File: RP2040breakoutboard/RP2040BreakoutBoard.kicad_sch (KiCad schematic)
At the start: 38 parts, among them J1 Conn_02x18_Odd_Even, J2 Conn_02x18_Odd_Even, J3 USB_C_Receptacle_USB2.0_14P, J4 Conn_01x02, U1 RP2040, U2 NCP1117-3.3_SOT223, U3 W25Q128JVS, X1 ABM8-272-T3

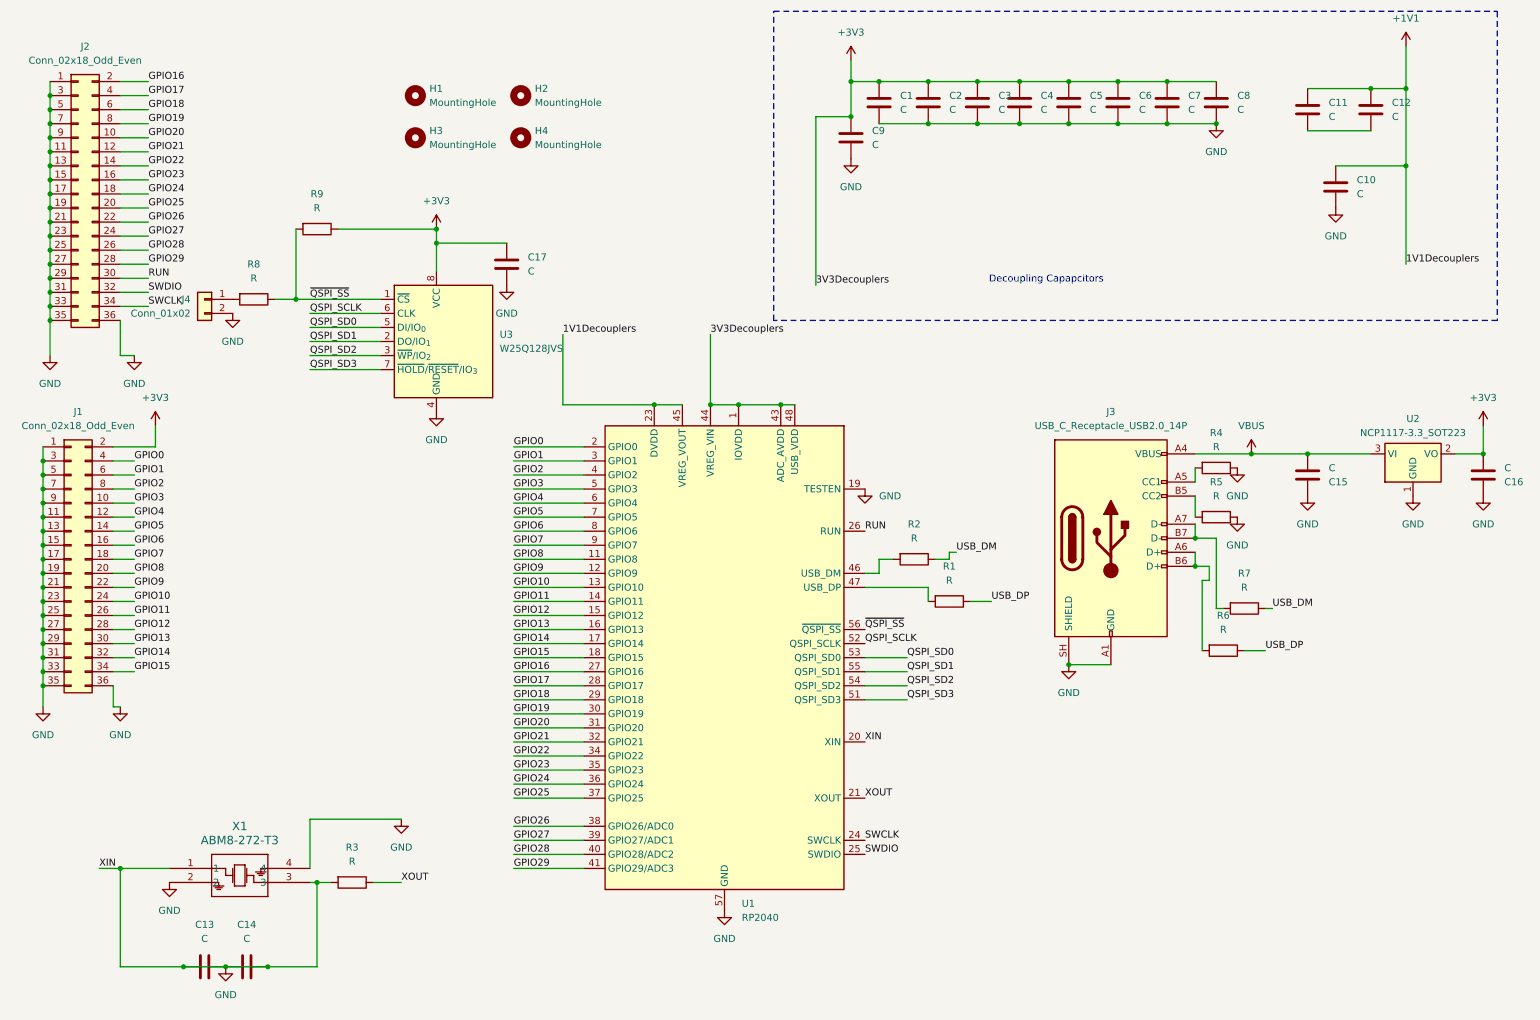
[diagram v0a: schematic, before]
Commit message: Tidied up schematic and assigned footprints
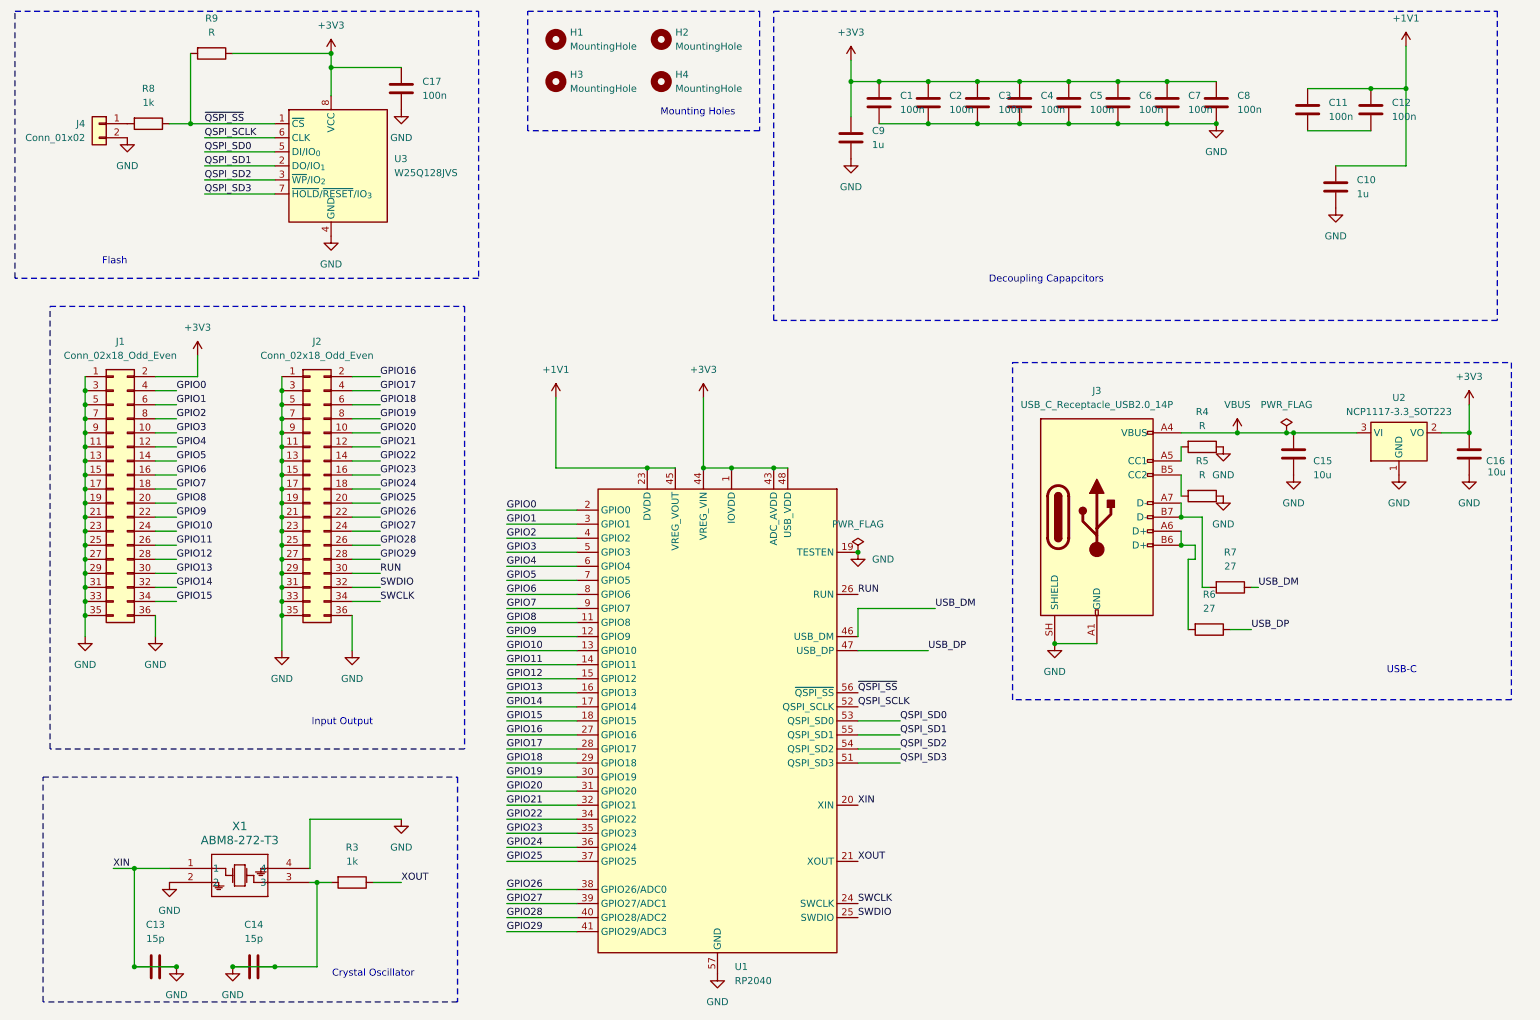
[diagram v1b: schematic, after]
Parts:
- removed R1, R2: R, symbol Device:R
- C1, C11, C12, C17, C2, C3, C4, C5, C6, C7, C8: value C -> 100n; footprint (none) -> Capacitor_SMD:C_0603_1608Metric
- C10, C9: value C -> 1u; footprint (none) -> Capacitor_SMD:C_0603_1608Metric
- C13, C14: value C -> 15p; footprint (none) -> Capacitor_SMD:C_0603_1608Metric
- C15, C16: value C -> 10u; footprint (none) -> Capacitor_SMD:C_0805_2012Metric
- H1, H2, H3, H4: footprint (none) -> MountingHole:MountingHole_3.2mm_M3
- J1, J2: footprint (none) -> Connector_PinHeader_2.54mm:PinHeader_2x18_P2.54mm_Vertical
- J3: footprint (none) -> Connector_USB:USB_C_Receptacle_GCT_USB4105-xx-A_16P_TopMnt_Horizontal
- J4: footprint (none) -> Connector_PinHeader_2.54mm:PinHeader_1x02_P2.54mm_Vertical
- R3, R8: value R -> 1k; footprint (none) -> Resistor_SMD:R_0603_1608Metric
- R4, R5, R9: footprint (none) -> Resistor_SMD:R_0603_1608Metric
- R6, R7: value R -> 27; footprint (none) -> Resistor_SMD:R_0603_1608Metric
- X1: footprint ABM8-272-T3_ABR -> Crystal:Crystal_SMD_3225-4Pin_3.2x2.5mm
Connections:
- net USB_DM: now also U1.46 (USB_DM)
- net USB_DP: now also U1.47 (USB_DP)
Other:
- note added: "Crystal Oscillator"
- note added: "Flash"
- note added: "Input Output"
- note added: "Mounting Holes"
- note added: "USB-C"
- moved on the sheet: C13, C14, C15, C16, C17, H1, H2, H3, H4, J1, J2, J3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

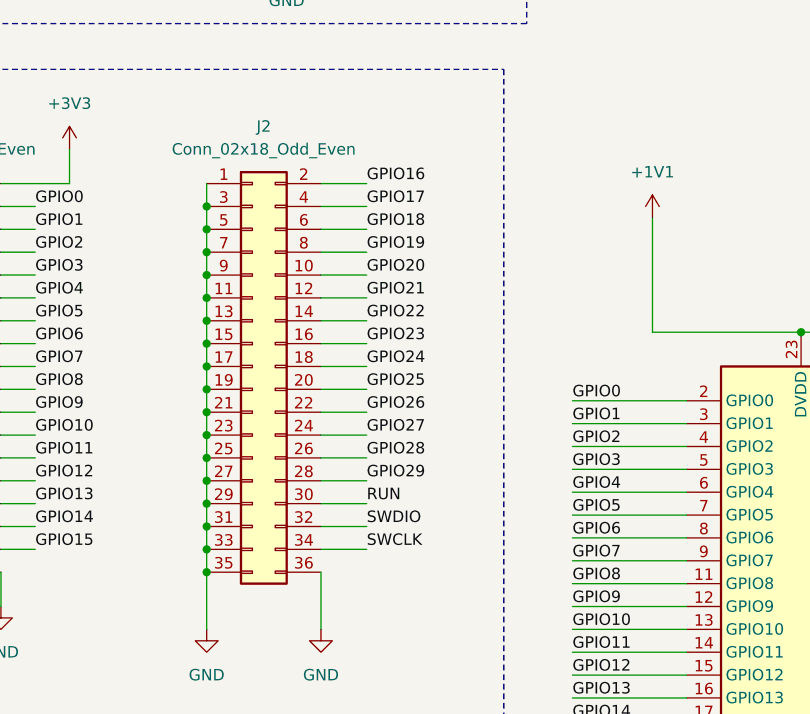
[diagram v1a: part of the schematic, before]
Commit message: Finished Component Placing
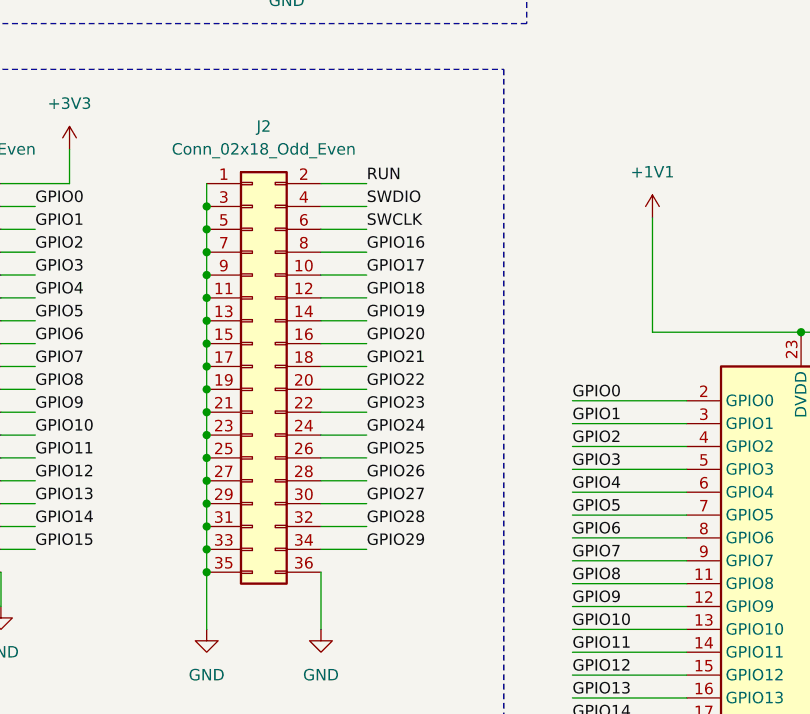
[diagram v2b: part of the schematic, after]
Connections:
- net GPIO16: now also J2.8 (Pin_8); no longer J2.2 (Pin_2)
- net GPIO17: now also J2.10 (Pin_10); no longer J2.4 (Pin_4)
- net GPIO18: now also J2.12 (Pin_12); no longer J2.6 (Pin_6)
- net GPIO19: now also J2.14 (Pin_14); no longer J2.8 (Pin_8)
- net GPIO20: now also J2.16 (Pin_16); no longer J2.10 (Pin_10)
- net GPIO21: now also J2.18 (Pin_18); no longer J2.12 (Pin_12)
- net GPIO22: now also J2.20 (Pin_20); no longer J2.14 (Pin_14)
- net GPIO23: now also J2.22 (Pin_22); no longer J2.16 (Pin_16)
- net GPIO24: now also J2.24 (Pin_24); no longer J2.18 (Pin_18)
- net GPIO25: now also J2.26 (Pin_26); no longer J2.20 (Pin_20)
- net GPIO26: now also J2.28 (Pin_28); no longer J2.22 (Pin_22)
- net GPIO27: now also J2.30 (Pin_30); no longer J2.24 (Pin_24)
- net GPIO28: now also J2.32 (Pin_32); no longer J2.26 (Pin_26)
- net GPIO29: now also J2.34 (Pin_34); no longer J2.28 (Pin_28)
- net RUN: now also J2.2 (Pin_2); no longer J2.30 (Pin_30)
- net SWCLK: now also J2.6 (Pin_6); no longer J2.34 (Pin_34)
- net SWDIO: now also J2.4 (Pin_4); no longer J2.32 (Pin_32)
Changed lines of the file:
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@@
-		)
-	)
-	(label "GPIO18"
-		(at 78.74 85.09 0)
-		(effects
-			(font
-				(size 1.27 1.27)
-			)
-			(justify left bottom)
 		)
 	)
@@
 		)
 	)
-	(label "GPIO19"
-		(at 78.74 87.63 0)
-		(effects
-			(font
-				(size 1.27 1.27)
-			)
-			(justify left bottom)
-		)
-	)
 	(label "QSPI_SCLK"
 		(at 165.1 139.7 0)
@@
 		)
 	)
-	(label "GPIO29"
-		(at 78.74 113.03 0)
-		(effects
-			(font
-				(size 1.27 1.27)
-			)
-			(justify left bottom)
-		)
-	)
-	(label "GPIO17"
-		(at 78.74 82.55 0)
-		(effects
-			(font
-				(size 1.27 1.27)
-			)
-			(justify left bottom)
-		)
-	)
 	(label "GPIO2"
 		(at 101.6 109.22 0)
@@
 		)
 	)
-	(label "GPIO28"
-		(at 78.74 110.49 0)
-		(effects
-			(font
-				(size 1.27 1.27)
-			)
-			(justify left bottom)
-		)
-	)
 	(label "GPIO7"
 		(at 101.6 121.92 0)
@@
 		)
 	)
+	(label "GPIO21"
+		(at 78.74 100.33 0)
+		(effects
+			(font
+				(size 1.27 1.27)
+			)
+			(justify left bottom)
+		)
+	)
+	(label "GPIO26"
+		(at 78.74 113.03 0)
+		(effects
+			(font
+				(size 1.27 1.27)
+			)
+			(justify left bottom)
+		)
+	)
 	(label "RUN"
 		(at 165.1 119.38 0)
@@
 		)
 	)
-	(label "GPIO16"
-		(at 78.74 80.01 0)
+	(label "GPIO27"
+		(at 78.74 115.57 0)
 		(effects
 			(font
@@
 		)
 	)
+	(label "GPIO18"
+		(at 78.74 92.71 0)
+		(effects
+			(font
+				(size 1.27 1.27)
+			)
+			(justify left bottom)
+		)
+	)
 	(label "USB_DM"
 		(at 237.49 118.11 0)
@@
 		)
 	)
+	(label "GPIO24"
+		(at 78.74 107.95 0)
+		(effects
+			(font
+				(size 1.27 1.27)
+			)
+			(justify left bottom)
+		)
+	)
 	(label "GPIO5"
 		(at 41.91 95.25 0)
@@
 		)
 	)
-	(label "GPIO26"
+	(label "GPIO23"
 		(at 78.74 105.41 0)
 		(effects
@@
 		)
 	)
-	(label "SWDIO"
-		(at 78.74 118.11 0)
-		(effects
-			(font
-				(size 1.27 1.27)
-			)
-			(justify left bottom)
-		)
-	)
 	(label "GPIO7"
 		(at 41.91 100.33 0)
@@
 		)
 	)
+	(label "GPIO22"
+		(at 78.74 102.87 0)
+		(effects
+			(font
+				(size 1.27 1.27)
+			)
+			(justify left bottom)
+		)
+	)
 	(label "GPIO13"
 		(at 41.91 115.57 0)
@@
 		)
 	)
-	(label "GPIO27"
-		(at 78.74 107.95 0)
-		(effects
-			(font
-				(size 1.27 1.27)
-			)
-			(justify left bottom)
-		)
-	)
 	(label "QSPI_SD2"
 		(at 172.72 147.32 0)
@@
 		)
 	)
-	(label "GPIO22"
-		(at 78.74 95.25 0)
-		(effects
-			(font
-				(size 1.27 1.27)
-			)
-			(justify left bottom)
-		)
-	)
 	(label "QSPI_SD2"
 		(at 46.99 44.45 0)
@@
 		)
 	)
-	(label "GPIO24"
-		(at 78.74 100.33 0)
-		(effects
-			(font
-				(size 1.27 1.27)
-			)
-			(justify left bottom)
-		)
-	)
 	(label "GPIO28"
 		(at 101.6 177.8 0)
@@
 		)
 	)
+	(label "GPIO25"
+		(at 78.74 110.49 0)
+		(effects
+			(font
+				(size 1.27 1.27)
+			)
+			(justify left bottom)
+		)
+	)
 	(label "XOUT"
 		(at 165.1 167.64 0)
@@
 		)
 	)
-	(label "GPIO23"
-		(at 78.74 97.79 0)
-		(effects
-			(font
-				(size 1.27 1.27)
-			)
-			(justify left bottom)
-		)
-	)
-	(label "GPIO25"
-		(at 78.74 102.87 0)
-		(effects
-			(font
-				(size 1.27 1.27)
-			)
-			(justify left bottom)
-		)
-	)
 	(label "XIN"
 		(at 30.48 168.91 0)
@@
 		)
 	)
+	(label "SWCLK"
+		(at 78.74 85.09 0)
+		(effects
+			(font
+				(size 1.27 1.27)
+			)
+			(justify left bottom)
+		)
+	)
 	(label "GPIO4"
 		(at 41.91 92.71 0)
@@
 		)
 	)
-	(label "RUN"
-		(at 78.74 115.57 0)
+	(label "GPIO29"
+		(at 78.74 120.65 0)
 		(effects
 			(font
@@
 		)
 	)
+	(label "GPIO16"
+		(at 78.74 87.63 0)
+		(effects
+			(font
+				(size 1.27 1.27)
+			)
+			(justify left bottom)
+		)
+	)
+	(label "GPIO28"
+		(at 78.74 118.11 0)
+		(effects
+			(font
+				(size 1.27 1.27)
+			)
+			(justify left bottom)
+		)
+	)
+	(label "GPIO17"
+		(at 78.74 90.17 0)
+		(effects
+			(font
+				(size 1.27 1.27)
+			)
+			(justify left bottom)
+		)
+	)
+	(label "GPIO19"
+		(at 78.74 95.25 0)
+		(effects
+			(font
+				(size 1.27 1.27)
+			)
+			(justify left bottom)
+		)
+	)
 	(label "GPIO27"
 		(at 101.6 175.26 0)
@@
 		)
 	)
+	(label "RUN"
+		(at 78.74 80.01 0)
+		(effects
+			(font
+				(size 1.27 1.27)
+			)
+			(justify left bottom)
+		)
+	)
 	(label "GPIO23"
 		(at 101.6 162.56 0)
@@
 		)
 	)
-	(label "GPIO21"
-		(at 78.74 92.71 0)
-		(effects
-			(font
-				(size 1.27 1.27)
-			)
-			(justify left bottom)
-		)
-	)
 	(label "GPIO1"
 		(at 41.91 85.09 0)
@@
 		)
 	)
+	(label "GPIO20"
+		(at 78.74 97.79 0)
+		(effects
+			(font
+				(size 1.27 1.27)
+			)
+			(justify left bottom)
+		)
+	)
 	(label "GPIO12"
 		(at 101.6 134.62 0)
@@
 		)
 	)
+	(label "SWDIO"
+		(at 78.74 82.55 0)
+		(effects
+			(font
+				(size 1.27 1.27)
+			)
+			(justify left bottom)
+		)
+	)
 	(label "GPIO5"
 		(at 101.6 116.84 0)
@@
 		)
 	)
-	(label "GPIO20"
-		(at 78.74 90.17 0)
-		(effects
-			(font
-				(size 1.27 1.27)
-			)
-			(justify left bottom)
-		)
-	)
 	(label "GPIO6"
 		(at 41.91 97.79 0)
 		(effects
 			(font
-				(size 1.27 1.27)
-			)
-			(justify left bottom)
-		)
-	)
-	(label "SWCLK"
-		(at 78.74 120.65 0)
-		(effects
-			(font

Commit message: Fixed Schematic
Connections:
- net +1V1: now also C11.2, C12.2
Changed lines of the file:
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@@
+	)
+	(junction
+		(at 257.81 35.56)
+		(diameter 0)
+		(color 0 0 0 0)
 	)
 	(junction
@@
 		(color 0 0 0 0)
 	)
+	(junction
+		(at 264.16 35.56)
+		(diameter 0)
+		(color 0 0 0 0)
+	)
 	(wire
 		(pts
@@
 	(wire
 		(pts
+			(xy 257.81 35.56) (xy 264.16 35.56)
+		)
+		(stroke
+			(width 0)
+			(type default)
+		)
+	)
+	(wire
+		(pts
 			(xy 227.33 105.41) (xy 223.52 105.41)
 		)
@@
 	(wire
 		(pts
+			(xy 264.16 35.56) (xy 264.16 27.94)
+		)
+		(stroke
+			(width 0)
+			(type default)
+		)
+	)
+	(wire
+		(pts
 			(xy 52.07 186.69) (xy 59.69 186.69)
 		)
@@
 	(wire
 		(pts
-			(xy 264.16 41.91) (xy 264.16 27.94)
-		)
-		(stroke
+			(xy 264.16 41.91) (xy 264.16 35.56)
+		)
+		(stroke

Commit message: Routed
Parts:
- removed R3: 1k, Resistor_SMD:R_0603_1608Metric, symbol Device:R
- removed X1: ABM8-272-T3, Crystal:Crystal_SMD_3225-4Pin_3.2x2.5mm, symbol ABM8-272-T3:ABM8-272-T3
- added Y2: Crystal_GND24, Crystal:Crystal_SMD_3225-4Pin_3.2x2.5mm, symbol Device:Crystal_GND24
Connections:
- net +1V1: no longer C11.2, C12.2
- net GND: now also C11.2, C12.2, Y2.2 (G), Y2.4 (G); no longer C13.2, C14.1, U1.20 (XIN)
- net RUN: now also J2.6 (Pin_6); no longer J2.2 (Pin_2)
- net SWCLK: now also J2.2 (Pin_2); no longer J2.6 (Pin_6)
- net XOUT: now also C14.1, Y2.3
- net USB_DM renamed USB_N
- net USB_DP renamed USB_P
- new net XIN: C13.2, U1.20 (XIN), Y2.1
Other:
- moved on the sheet: C10, C11, C12, C13, C14, C9
